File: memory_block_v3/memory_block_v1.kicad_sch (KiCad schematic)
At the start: 14 parts, among them J1 4677, J11 Conn_01x07, J2 DM3D-SF, J3 Conn_01x02, J4 Conn_01x19, J5 Conn_01x03, J6 Conn_01x19, J7 Conn_01x03, U1 ESP32-WROOM-32E-N8, U2 W25Q128JVSIQ TR

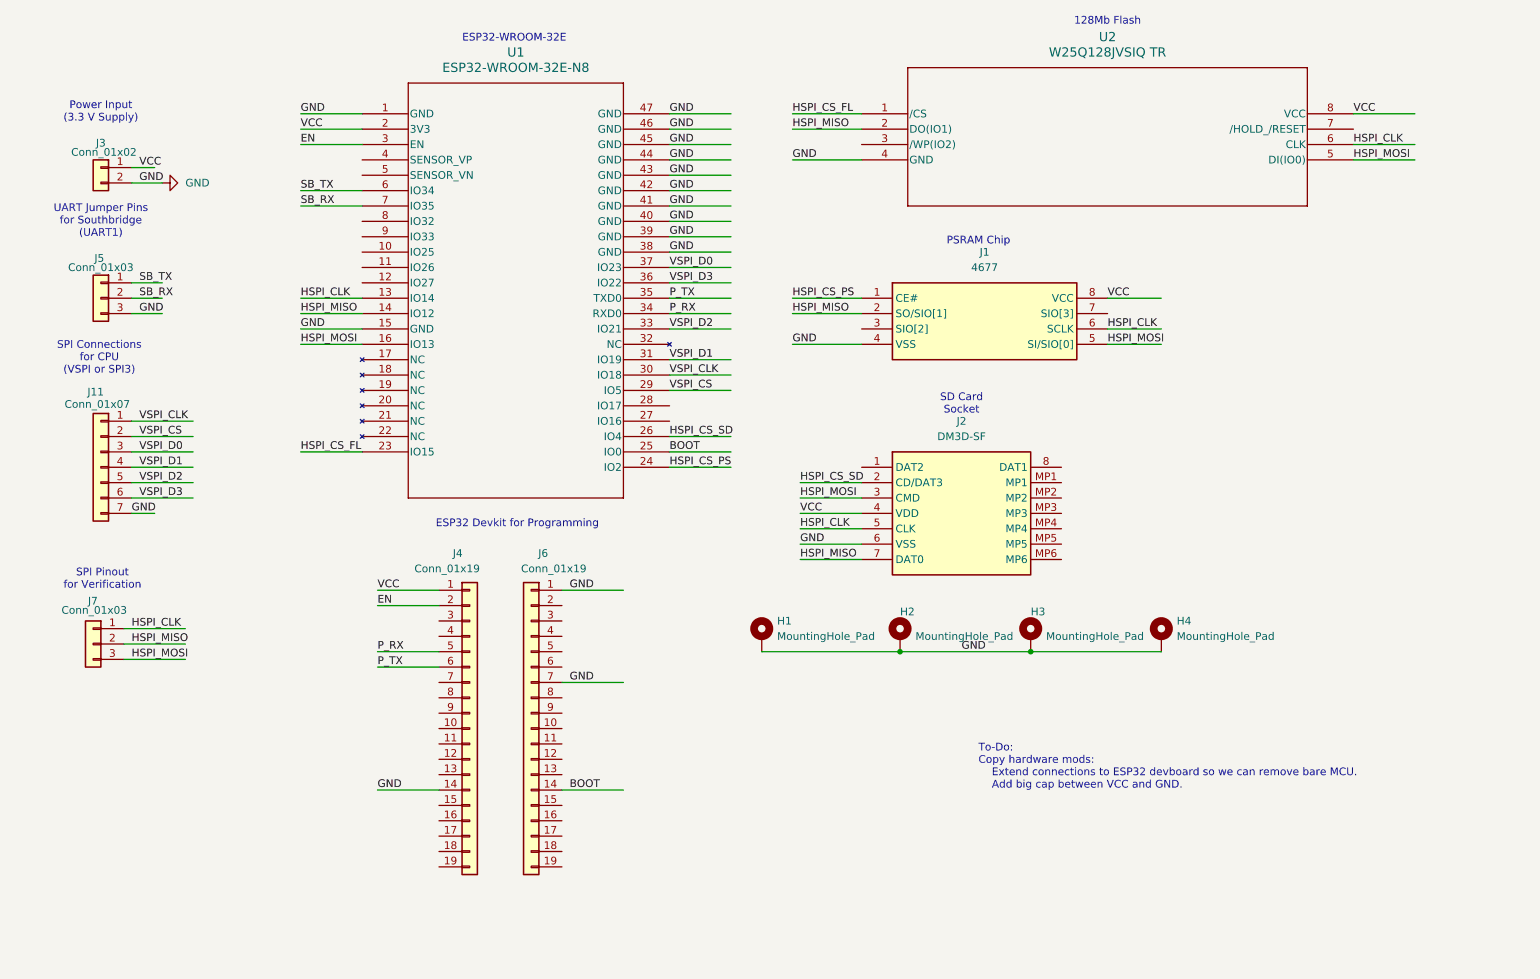
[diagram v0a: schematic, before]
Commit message: pt1 NB/MB repairs
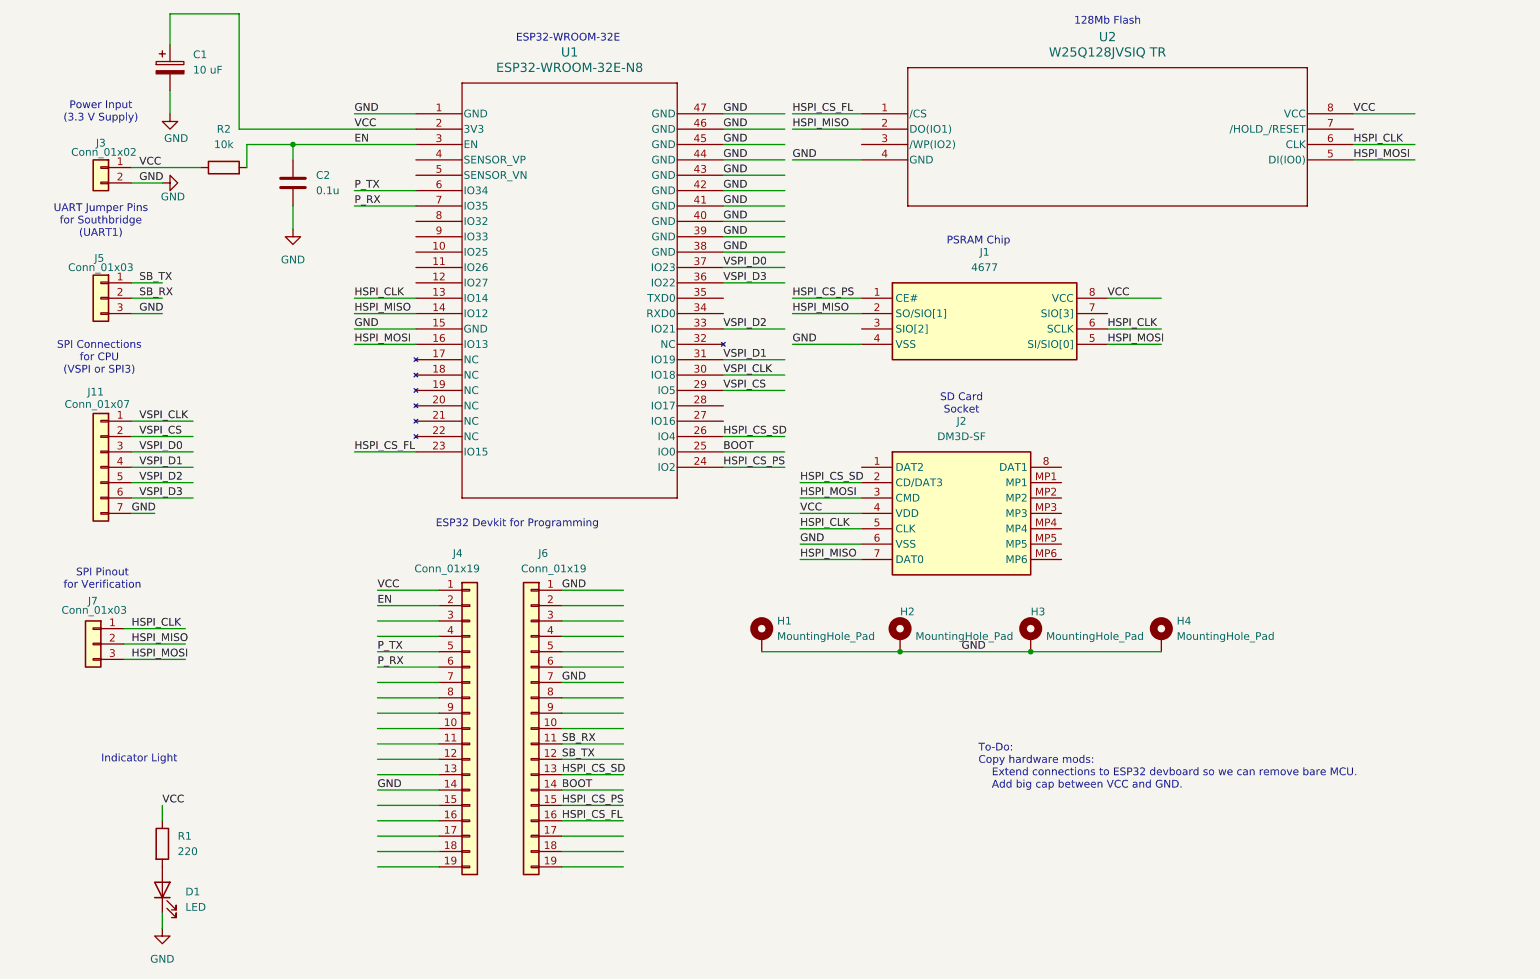
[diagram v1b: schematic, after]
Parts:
- added C1: 10 uF, Capacitor_THT:CP_Radial_D10.0mm_P2.50mm, symbol Device:C_Polarized
- added C2: 0.1u, Capacitor_THT:C_Rect_L7.5mm_W6.5mm_P5.00mm, symbol Device:C
- added D1: LED, symbol Device:LED
- added R1: 220, Resistor_THT:R_Axial_DIN0207_L6.3mm_D2.5mm_P7.62mm_Horizontal, symbol Device:R
- added R2: 10k, Resistor_THT:R_Axial_DIN0207_L6.3mm_D2.5mm_P7.62mm_Horizontal, symbol Device:R
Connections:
- net HSPI_CS_FL is gone; now on net GND: U1.23 (IO15), U2.1 (/CS)
- net HSPI_CS_PS is gone; now on net GND: J1.1 (CE#), U1.24 (IO2)
- net SB_RX is gone; now on net GND: J5.2 (Pin_2), U1.7 (IO35)
- net SB_TX is gone; now on net GND: J5.1 (Pin_1), U1.6 (IO34)
- net GND: now also J4.10 (Pin_10), J4.11 (Pin_11), J4.12 (Pin_12), J4.13 (Pin_13), J4.15 (Pin_15), J4.16 (Pin_16), J4.17 (Pin_17), J4.18 (Pin_18), J4.19 (Pin_19), J4.3 (Pin_3), J4.4 (Pin_4), J4.7 (Pin_7), J4.8 (Pin_8), J4.9 (Pin_9), C1.1, C1.2, C2.1, C2.2, D1.1 (K), R1.1, R2.1, R2.2; no longer U1.34 (RXD0), U1.35 (TXD0)
- new net: D1.2 (A), R1.2
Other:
- note added: "Indicator Light"
- moved on the sheet: U1

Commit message: First Draft NB/MB Schematic
PCB has yet to be updated, but added enable strapping resistor, power LED, and power-stabilizing capacitor. Next plans are implementing these changes on a 4-layer PCB.
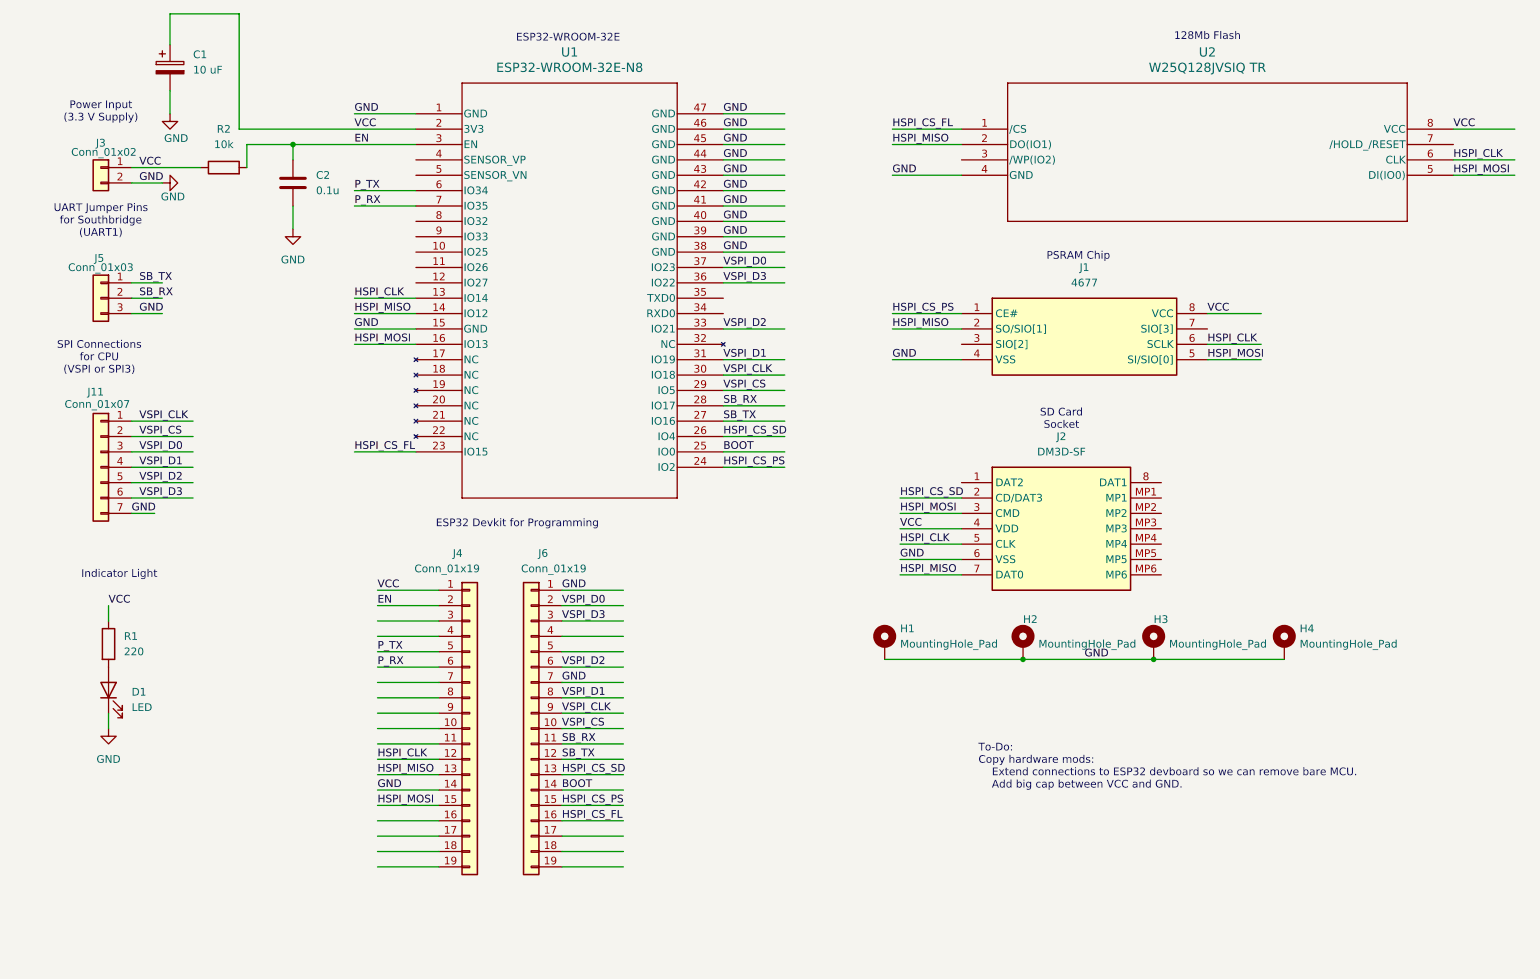
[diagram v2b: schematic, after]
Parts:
- removed J7: Conn_01x03, Connector_PinSocket_2.54mm:PinSocket_1x03_P2.54mm_Vertical, symbol Connector_Generic:Conn_01x03
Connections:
- net GND: now also U1.27 (IO16), U1.28 (IO17)
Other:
- note removed: "SPI Pinout for Verification"
- moved on the sheet: D1, H1, H2, H3, H4, J1, J2, R1, U2

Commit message: Start of NB/MB PCB Rework
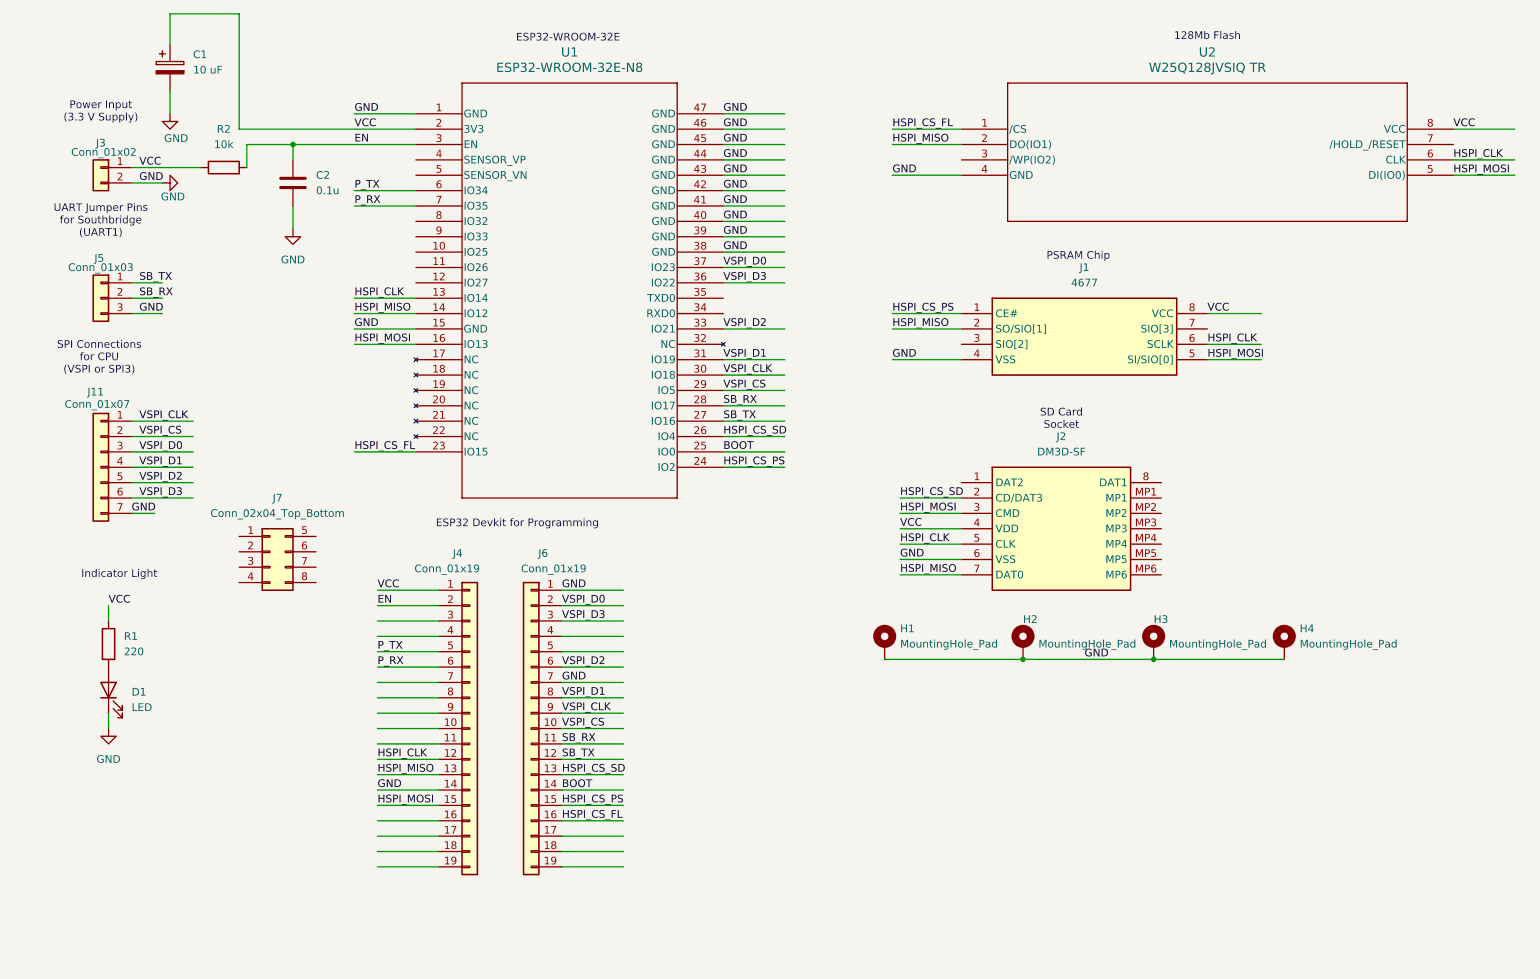
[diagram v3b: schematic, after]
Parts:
- added J7: Conn_02x04_Top_Bottom, symbol Connector_Generic:Conn_02x04_Top_Bottom
- D1: footprint (none) -> LED_THT:LED_D3.0mm
- J11: footprint Connector_PinSocket_2.54mm:PinSocket_1x07_P2.54mm_Vertical -> Connector_PinSocket_2.54mm:PinSocket_1x07_P2.54mm_Horizontal
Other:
- note removed: "To-Do: Copy hardware mods: Extend connections to ESP32 devboard so we can remove bare MCU. Add big cap between VCC and GND."
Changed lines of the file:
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@@
 		)
 	)
-	(text "To-Do:\nCopy hardware mods:\n	Extend connections to ESP32 devboard so we can remove bare MCU.\n	Add big cap between VCC and GND.\n"
-		(exclude_from_sim no)
-		(at 169.164 140.97 0)
-		(effects
-			(font
-				(size 1.27 1.27)
-			)
-			(justify left)
-		)
-	)
 	(text "ESP32 Devkit for Programming"
 		(exclude_from_sim no)
@@
 			)
 		)
-		(property "Footprint" "Connector_PinSocket_2.54mm:PinSocket_1x07_P2.54mm_Vertical"
+		(property "Footprint" "Connector_PinSocket_2.54mm:PinSocket_1x07_P2.54mm_Horizontal"
 			(at 24.13 91.44 0)
 			(effects
@@
 	)
 	(symbol
+		(lib_id "Connector_Generic:Conn_02x04_Top_Bottom")
+		(at 52.07 105.41 0)
+		(unit 1)
+		(exclude_from_sim no)
+		(in_bom yes)
+		(on_board yes)
+		(dnp no)
+		(fields_autoplaced yes)
+		(property "Reference" "J7"
+			(at 53.34 96.52 0)
+			(effects
+				(font
+					(size 1.27 1.27)
+				)
+			)
+		)
+		(property "Value" "Conn_02x04_Top_Bottom"
+			(at 53.34 99.06 0)
+			(effects
+				(font
+					(size 1.27 1.27)
+				)
+			)
+		)
+		(property "Footprint" ""
+			(at 52.07 105.41 0)
+			(effects
+				(font
+					(size 1.27 1.27)
+				)
+				(hide yes)
+			)
+		)
+		(property "Datasheet" "~"
+			(at 52.07 105.41 0)
+			(effects
+				(font
+					(size 1.27 1.27)
+				)
+				(hide yes)
+			)
+		)
+		(property "Description" "Generic connector, double row, 02x04, top/bottom pin numbering scheme (row 1: 1...pins_per_row, row2: pins_per_row+1 ... num_pins), script generated (kicad-library-utils/schlib/autogen/connector/)"
+			(at 52.07 105.41 0)
+			(effects
+				(font
+					(size 1.27 1.27)
+				)
+				(hide yes)
+			)
+		)
+		(pin "1"
+		)
+		(pin "4"
+		)
+		(pin "3"
+		)
+		(pin "8"
+		)
+		(pin "5"
+		)
+		(pin "6"
+		)
+		(pin "7"
+		)
+		(pin "2"
+		)
+		(instances
+			(project ""
+				(path "/bcf8a956-bdd4-49e6-840a-35b0933db3f2"
+					(reference "J7")
+					(unit 1)
+				)
+			)
+		)
+	)
+	(symbol
 		(lib_id "Device:LED")
 		(at 25.4 128.27 90)
@@
 			)
 		)
-		(property "Footprint" ""
+		(property "Footprint" "LED_THT:LED_D3.0mm"
 			(at 25.4 128.27 0)
 			(effects

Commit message: continued NB/MB pcb progress
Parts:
- removed J11: Conn_01x07, Connector_PinSocket_2.54mm:PinSocket_1x07_P2.54mm_Horizontal, symbol Connector_Generic:Conn_01x07
- removed J5: Conn_01x03, Connector_PinSocket_2.54mm:PinSocket_1x03_P2.54mm_Vertical, symbol Connector_Generic:Conn_01x03
- removed J7: Conn_02x04_Top_Bottom, symbol Connector_Generic:Conn_02x04_Top_Bottom
- added J5: Conn_01x04, Connector_PinHeader_2.54mm:PinHeader_1x04_P2.54mm_Horizontal, symbol Connector_Generic:Conn_01x04
- added J7: Conn_02x05_Odd_Even, Connector_PinHeader_2.54mm:PinHeader_2x05_P2.54mm_Horizontal, symbol Connector_Generic:Conn_02x05_Odd_Even
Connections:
- net GND: now also J5.1 (Pin_1), J5.2 (Pin_2), J5.3 (Pin_3), J5.4 (Pin_4), J7.1 (Pin_1), J7.10 (Pin_10), J7.2 (Pin_2), J7.3 (Pin_3), J7.4 (Pin_4), J7.5 (Pin_5), J7.7 (Pin_7)
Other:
- moved on the sheet: D1, R1

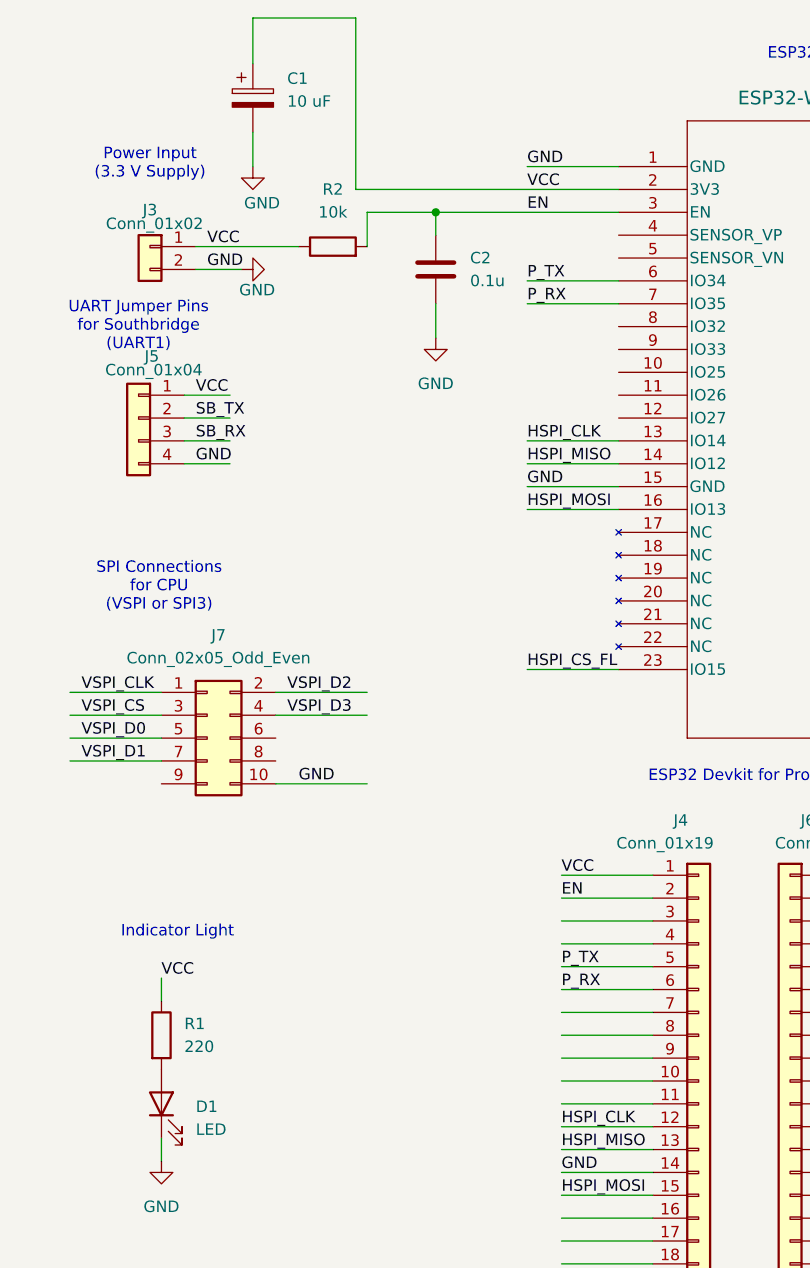
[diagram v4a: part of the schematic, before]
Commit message: Changed header pins, redone PCB layout
Still need to do actual trace routing, but have general components mapped out.
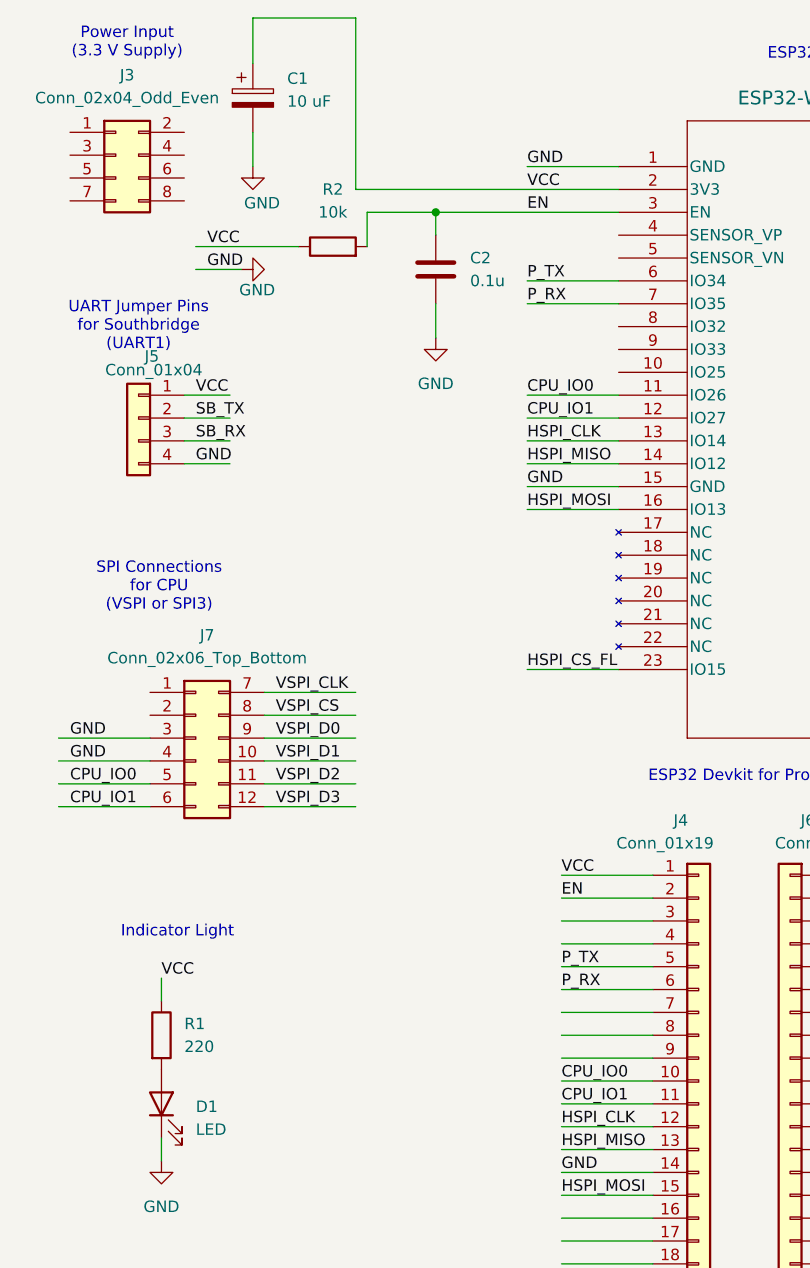
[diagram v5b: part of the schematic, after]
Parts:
- removed J3: Conn_01x02, Connector_PinSocket_2.54mm:PinSocket_1x02_P2.54mm_Vertical, symbol Connector_Generic:Conn_01x02
- removed J7: Conn_02x05_Odd_Even, Connector_PinHeader_2.54mm:PinHeader_2x05_P2.54mm_Horizontal, symbol Connector_Generic:Conn_02x05_Odd_Even
- added J3: Conn_02x04_Odd_Even, Connector_PinHeader_2.54mm:PinHeader_2x04_P2.54mm_Vertical, symbol Connector_Generic:Conn_02x04_Odd_Even
- added J7: Conn_02x06_Top_Bottom, Connector_PinHeader_2.54mm:PinHeader_2x06_P2.54mm_Horizontal, symbol Connector_Generic:Conn_02x06_Top_Bottom
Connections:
- net GND: now also U1.11 (IO26), U1.12 (IO27), J7.10 (Pin_10), J7.11 (Pin_11), J7.12 (Pin_12), J7.3 (Pin_3), J7.4 (Pin_4), J7.5 (Pin_5), J7.6 (Pin_6), J7.7 (Pin_7), J7.8 (Pin_8), J7.9 (Pin_9)
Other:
- title: (none) -> Northbridge & Memory Block
